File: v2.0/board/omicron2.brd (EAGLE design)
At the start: 76.2 x 53.3 mm, 195 parts, among them IC1 XC6SLX4-1876221, IC2 TPS73033DBV-1135395, IC3 LD6806TD/12H-2095494, IC4 H57V2562GTR-75C-1907383, IC5 M25P40-2253716, IC6 TPS73033DBV-1135395, Q1 PDTC123-1757992, Q2 BC807W, Q3 PDTC123-1757992, Q4 BC807W, X1 USB-MICRO-B-BOTTOM, X2 7C-33.3-1842039

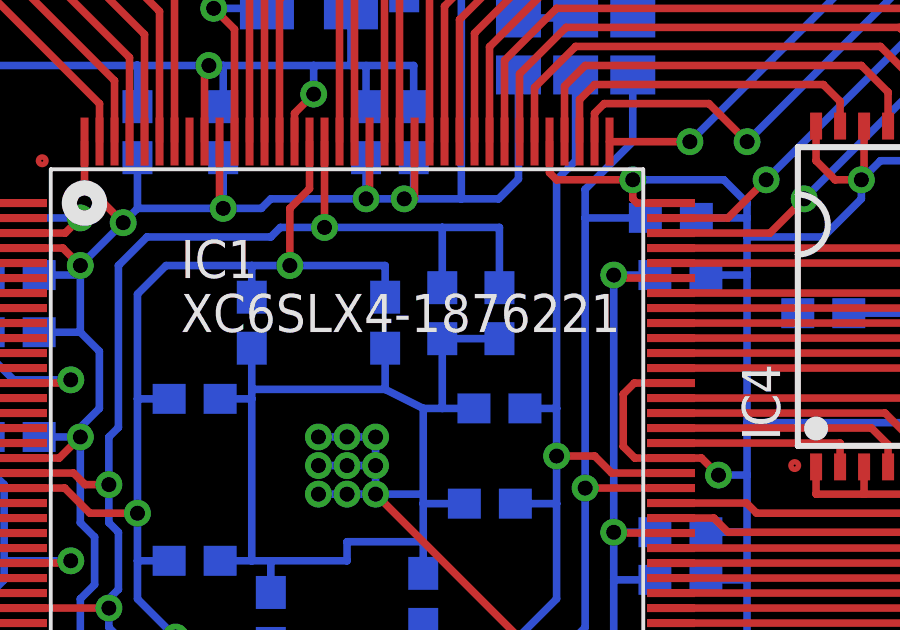
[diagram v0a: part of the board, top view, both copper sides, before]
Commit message: Changed the device to 6slx9; added board errata
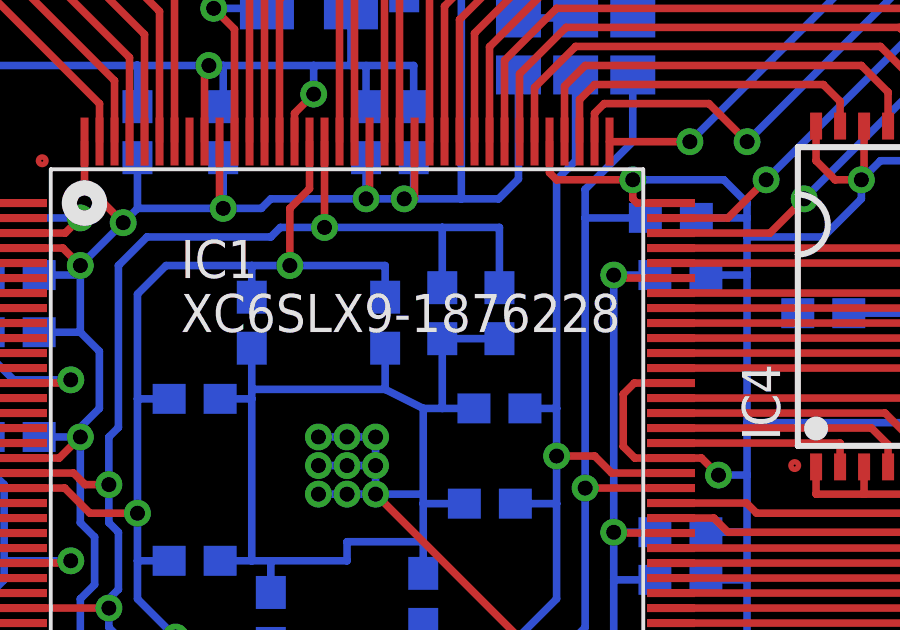
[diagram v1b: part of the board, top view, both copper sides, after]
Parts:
- IC1: value XC6SLX4-1876221 -> XC6SLX9-1876228
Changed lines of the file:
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@@
 <?xml version="1.0" encoding="utf-8"?>
 <!DOCTYPE eagle SYSTEM "eagle.dtd">
-<eagle version="6.3">
+<eagle version="7.0.0">
 <drawing>
 <settings>
@@
 <pass name="Default">
 <param name="RoutingGrid" value="50mil"/>
+<param name="AutoGrid" value="1"/>
+<param name="Efforts" value="0"/>
+<param name="TopRouterVariant" value="1"/>
 <param name="tpViaShape" value="round"/>
 <param name="PrefDir.1" value="|"/>
@@
 </autorouter>
 <elements>
-<element name="IC1" library="xilinx" package="TQG144" value="XC6SLX4-1876221" x="34.925" y="27.305"/>
+<element name="IC1" library="xilinx" package="TQG144" value="XC6SLX9-1876228" x="34.925" y="27.305"/>
 <element name="X1" library="usb" package="USB-MICRO-B-BOTTOM-MOLEX" value="USB-MICRO-B-BOTTOM" x="74.93" y="26.67" rot="MR0"/>
 <element name="IC2" library="tps73033" package="SOT23-DBV" value="TPS73033DBV-1135395" x="43.18" y="48.26" rot="MR180"/>
